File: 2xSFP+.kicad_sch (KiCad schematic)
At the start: 55 parts, among them J2 SFP+_Bel_SS-79100-010, U5 PCA9539AHF

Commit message: Update symbols from the library
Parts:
- J2: footprint antmicro-footprints:SFP_SS-79100-010 -> antmicro-footprints:SFP+_SS-79100-010
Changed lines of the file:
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@@
+    )
+  )
+  (symbol (lib_id "antmicroEdgeConnectors:SFP+_Bel_SS-79100-010") (at 261.62 60.96 0) (unit 1)
+    (in_bom yes) (on_board yes) (dnp no) (fields_autoplaced)
+    (property "Reference" "J2" (at 275.59 53.34 0)
+      (effects (font (size 1.27 1.27) (thickness 0.15)))
+    )
+    (property "Value" "SFP+_Bel_SS-79100-010" (at 303.53 73.66 0)
+      (effects (font (size 1.27 1.27) (thickness 0.15)) (justify left bottom) hide)
+    )
+    (property "Footprint" "antmicro-footprints:SFP+_SS-79100-010" (at 303.53 76.2 0)
+      (effects (font (size 1.27 1.27) (thickness 0.15)) (justify left bottom) hide)
+    )
+    (property "Datasheet" "https://www.belfuse.com/resources/datasheets/stewartconnector/ds-STW-SFP-cages.pdf" (at 303.53 78.74 0)
+      (effects (font (size 1.27 1.27) (thickness 0.15)) (justify left bottom) hide)
+    )
+    (property "MPN" "SS-79100-010" (at 275.59 55.88 0)
+      (effects (font (size 1.27 1.27) (thickness 0.15)))
+    )
+    (property "Manufacturer" "Bel Fuse" (at 303.53 68.58 0)
+      (effects (font (size 1.27 1.27) (thickness 0.15)) (justify left bottom) hide)
+    )
+    (property "Author" "Antmicro" (at 303.53 81.28 0)
+      (effects (font (size 1.27 1.27) (thickness 0.15)) (justify left bottom) hide)
+    )
+    (property "License" "Apache-2.0" (at 303.53 83.82 0)
+      (effects (font (size 1.27 1.27) (thickness 0.15)) (justify left bottom) hide)
+    )
+    (pin "B9")
+    (pin "T9")
+    (pin "B6")
+    (pin "B16")
+    (pin "T8")
+    (pin "B13")
+    (pin "T6")
+    (pin "B18")
+    (pin "B4")
+    (pin "B19")
+    (pin "T14")
+    (pin "T11")
+    (pin "T10")
+    (pin "T12")
+    (pin "T3")
+    (pin "B17")
+    (pin "T19")
+    (pin "T20")
+    (pin "B3")
+    (pin "B10")
+    (pin "B11")
+    (pin "T17")
+    (pin "T7")
+    (pin "B5")
+    (pin "B8")
+    (pin "B15")
+    (pin "B7")
+    (pin "T2")
+    (pin "T13")
+    (pin "T5")
+    (pin "T18")
+    (pin "B14")
+    (pin "B2")
+    (pin "B20")
+    (pin "T16")
+    (pin "T4")
+    (pin "B1")
+    (pin "T15")
+    (pin "B12")
+    (pin "SH")
+    (pin "T1")
+    (instances
+      (project "com-express-7-baseboard"
+        (path "/1b8c34da-dad5-4b0b-8c4b-45db766c4dfa/bc90cc14-34f1-4905-9b90-ab809e861ec6"
+          (reference "J2") (unit 1)
+        )
+      )
     )
   )
@@
     )
   )
-  (symbol (lib_id "antmicroEdgeConnectors:SFP+_Bel_SS-79100-010") (at 261.62 60.96 0) (unit 1)
-    (in_bom yes) (on_board yes) (dnp no) (fields_autoplaced)
-    (property "Reference" "J2" (at 275.59 53.34 0)
-      (effects (font (size 1.27 1.27) (thickness 0.15)))
-    )
-    (property "Value" "SFP+_Bel_SS-79100-010" (at 303.53 73.66 0)
-      (effects (font (size 1.27 1.27) (thickness 0.15)) (justify left bottom) hide)
-    )
-    (property "Footprint" "antmicro-footprints:SFP_SS-79100-010" (at 303.53 76.2 0)
-      (effects (font (size 1.27 1.27) (thickness 0.15)) (justify left bottom) hide)
-    )
-    (property "Datasheet" "https://www.belfuse.com/resources/datasheets/stewartconnector/ds-STW-SFP-cages.pdf" (at 303.53 78.74 0)
-      (effects (font (size 1.27 1.27) (thickness 0.15)) (justify left bottom) hide)
-    )
-    (property "MPN" "SS-79100-010" (at 275.59 55.88 0)
-      (effects (font (size 1.27 1.27) (thickness 0.15)))
-    )
-    (property "Manufacturer" "Bel Fuse" (at 303.53 68.58 0)
-      (effects (font (size 1.27 1.27) (thickness 0.15)) (justify left bottom) hide)
-    )
-    (property "Author" "Antmicro" (at 303.53 81.28 0)
-      (effects (font (size 1.27 1.27) (thickness 0.15)) (justify left bottom) hide)
-    )
-    (property "License" "Apache-2.0" (at 303.53 83.82 0)
-      (effects (font (size 1.27 1.27) (thickness 0.15)) (justify left bottom) hide)
-    )
-    (pin "T4")
-    (pin "B13")
-    (pin "B16")
-    (pin "B15")
-    (pin "B19")
-    (pin "B20")
-    (pin "T11")
-    (pin "B4")
-    (pin "B9")
-    (pin "B18")
-    (pin "B6")
-    (pin "T8")
-    (pin "B12")
-    (pin "B17")
-    (pin "T2")
-    (pin "B14")
-    (pin "B5")
-    (pin "B7")
-    (pin "T19")
-    (pin "B1")
-    (pin "T18")
-    (pin "B8")
-    (pin "T20")
-    (pin "B2")
-    (pin "T17")
-    (pin "T9")
-    (pin "T5")
-    (pin "T15")
-    (pin "T7")
-    (pin "B11")
-    (pin "T6")
-    (pin "B10")
-    (pin "T12")
-    (pin "T3")
-    (pin "T16")
-    (pin "B3")
-    (pin "T1")
-    (pin "T10")
-    (pin "SH")
-    (pin "T13")
-    (pin "T14")
-    (instances
-      (project "com-express-7-baseboard"
-        (path "/1b8c34da-dad5-4b0b-8c4b-45db766c4dfa/bc90cc14-34f1-4905-9b90-ab809e861ec6"
-          (reference "J2") (unit 1)
-        )
-      )
-    )
-  )
   (symbol (lib_id "antmicropower:+3V3") (at 322.58 69.85 0) (unit 1)
     (in_bom yes) (on_board yes) (dnp no)
@@
     )
   )
+  (symbol (lib_id "antmicroEdgeConnectors:SFP+_Bel_SS-79100-010") (at 261.62 144.78 0) (unit 2)
+    (in_bom yes) (on_board yes) (dnp no) (fields_autoplaced)
+    (property "Reference" "J2" (at 275.59 137.16 0)
+      (effects (font (size 1.27 1.27) (thickness 0.15)))
+    )
+    (property "Value" "SFP+_Bel_SS-79100-010" (at 303.53 157.48 0)
+      (effects (font (size 1.27 1.27) (thickness 0.15)) (justify left bottom) hide)
+    )
+    (property "Footprint" "antmicro-footprints:SFP+_SS-79100-010" (at 303.53 160.02 0)
+      (effects (font (size 1.27 1.27) (thickness 0.15)) (justify left bottom) hide)
+    )
+    (property "Datasheet" "https://www.belfuse.com/resources/datasheets/stewartconnector/ds-STW-SFP-cages.pdf" (at 303.53 162.56 0)
+      (effects (font (size 1.27 1.27) (thickness 0.15)) (justify left bottom) hide)
+    )
+    (property "MPN" "SS-79100-010" (at 275.59 139.7 0)
+      (effects (font (size 1.27 1.27) (thickness 0.15)))
+    )
+    (property "Manufacturer" "Bel Fuse" (at 303.53 152.4 0)
+      (effects (font (size 1.27 1.27) (thickness 0.15)) (justify left bottom) hide)
+    )
+    (property "Author" "Antmicro" (at 303.53 165.1 0)
+      (effects (font (size 1.27 1.27) (thickness 0.15)) (justify left bottom) hide)
+    )
+    (property "License" "Apache-2.0" (at 303.53 167.64 0)
+      (effects (font (size 1.27 1.27) (thickness 0.15)) (justify left bottom) hide)
+    )
+    (pin "B9")
+    (pin "T9")
+    (pin "B6")
+    (pin "B16")
+    (pin "T8")
+    (pin "B13")
+    (pin "T6")
+    (pin "B18")
+    (pin "B4")
+    (pin "B19")
+    (pin "T14")
+    (pin "T11")
+    (pin "T10")
+    (pin "T12")
+    (pin "T3")
+    (pin "B17")
+    (pin "T19")
+    (pin "T20")
+    (pin "B3")
+    (pin "B10")
+    (pin "B11")
+    (pin "T17")
+    (pin "T7")
+    (pin "B5")
+    (pin "B8")
+    (pin "B15")
+    (pin "B7")
+    (pin "T2")
+    (pin "T13")
+    (pin "T5")
+    (pin "T18")
+    (pin "B14")
+    (pin "B2")
+    (pin "B20")
+    (pin "T16")
+    (pin "T4")
+    (pin "B1")
+    (pin "T15")
+    (pin "B12")
+    (pin "SH")
+    (pin "T1")
+    (instances
+      (project "com-express-7-baseboard"
+        (path "/1b8c34da-dad5-4b0b-8c4b-45db766c4dfa/bc90cc14-34f1-4905-9b90-ab809e861ec6"
+          (reference "J2") (unit 2)
+        )
+      )
+    )
+  )
   (symbol (lib_id "antmicropower:GND") (at 177.8 274.32 0) (unit 1)
     (in_bom yes) (on_board yes) (dnp no)
@@
         )
       )
-    )
-  )
-  (symbol (lib_id "antmicroEdgeConnectors:SFP+_Bel_SS-79100-010") (at 261.62 144.78 0) (unit 2)
-    (in_bom yes) (on_board yes) (dnp no)
-    (property "Reference" "J2" (at 275.59 137.16 0)
-      (effects (font (size 1.27 1.27) (thickness 0.15)))
-    )
-    (property "Value" "SFP+_Bel_SS-79100-010" (at 303.53 157.48 0)
-      (effects (font (size 1.27 1.27) (thickness 0.15)) (justify left bottom) hide)
-    )
-    (property "Footprint" "antmicro-footprints:SFP_SS-79100-010" (at 303.53 160.02 0)
-      (effects (font (size 1.27 1.27) (thickness 0.15)) (justify left bottom) hide)
-    )
-    (property "Datasheet" "https://www.belfuse.com/resources/datasheets/stewartconnector/ds-STW-SFP-cages.pdf" (at 303.53 162.56 0)
-      (effects (font (size 1.27 1.27) (thickness 0.15)) (justify left bottom) hide)
-    )
-    (property "MPN" "SS-79100-010" (at 275.59 139.7 0)
-      (effects (font (size 1.27 1.27) (thickness 0.15)))
-    )
-    (property "Manufacturer" "Bel Fuse" (at 303.53 152.4 0)
-      (effects (font (size 1.27 1.27) (thickness 0.15)) (justify left bottom) hide)
-    )
-    (property "Author" "Antmicro" (at 303.53 165.1 0)
-      (effects (font (size 1.27 1.27) (thickness 0.15)) (justify left bottom) hide)
-    )
-    (property "License" "Apache-2.0" (at 303.53 167.64 0)
-      (effects (font (size 1.27 1.27) (thickness 0.15)) (justify left bottom) hide)
-    )
-    (pin "T4")
-    (pin "B13")
-    (pin "B16")
-    (pin "B15")
-    (pin "B19")
-    (pin "B20")
-    (pin "T11")
-    (pin "B4")
-    (pin "B9")
-    (pin "B18")
-    (pin "B6")
-    (pin "T8")
-    (pin "B12")
-    (pin "B17")
-    (pin "T2")
-    (pin "B14")
-    (pin "B5")
-    (pin "B7")
-    (pin "T19")
-    (pin "B1")
-    (pin "T18")
-    (pin "B8")
-    (pin "T20")
-    (pin "B2")
-    (pin "T17")
-    (pin "T9")
-    (pin "T5")
-    (pin "T15")
-    (pin "T7")
-    (pin "B11")
-    (pin "T6")
-    (pin "B10")
-    (pin "T12")
-    (pin "T3")
-    (pin "T16")
-    (pin "B3")
-    (pin "T1")
-    (pin "T10")
-    (pin "SH")
-    (pin "T13")
-    (pin "T14")
-    (instances
-      (project "com-express-7-baseboard"
-        (path "/1b8c34da-dad5-4b0b-8c4b-45db766c4dfa/bc90cc14-34f1-4905-9b90-ab809e861ec6"
-          (reference "J2") (unit 2)
-        )
-      )

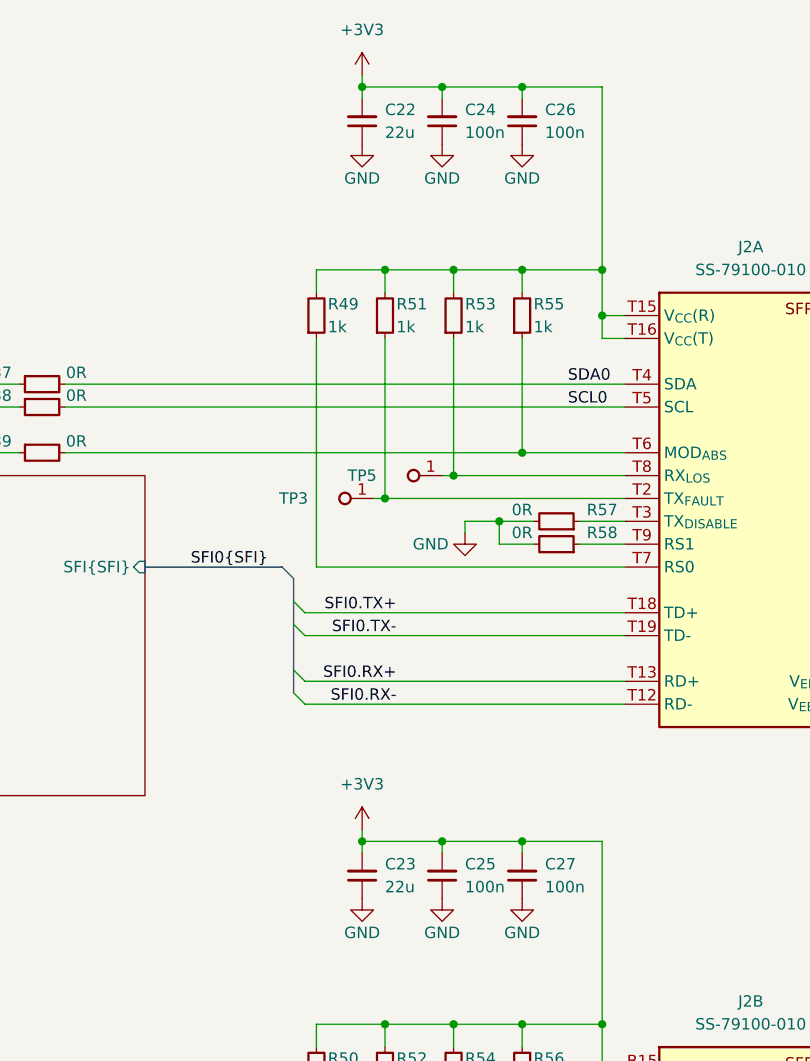
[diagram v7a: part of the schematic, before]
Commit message: [#58137] Add DC/DC supplies
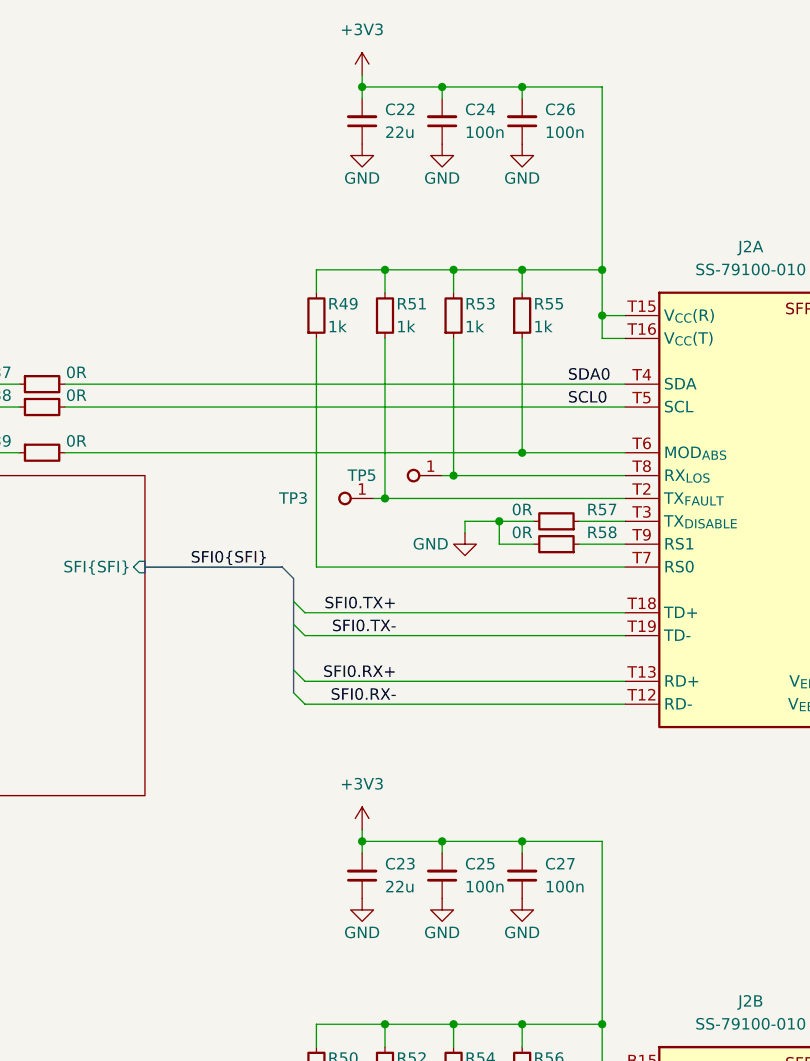
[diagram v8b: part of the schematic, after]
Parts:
- C22, C23: value C_22u_0603 -> C_22u_16V_0603; symbol antmicroCapacitors0603:C_22u_0603 -> antmicroCapacitors0603:C_22u_16V_0603; MPN GRM188R60J226MEA0D -> CL10A226MO7JZNC; Manufacturer Murata -> Samsung Electro-Mechanics; Voltage (none) -> 16V
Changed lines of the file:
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@@
     )
   )
-  (symbol (lib_id "antmicroCapacitors0603:C_22u_0603") (at 232.41 125.73 90) (unit 1)
+  (symbol (lib_id "antmicroCapacitors0603:C_22u_16V_0603") (at 232.41 125.73 90) (unit 1)
     (in_bom yes) (on_board yes) (dnp no) (fields_autoplaced)
-    (property "Reference" "C23" (at 234.95 121.9136 90)
-      (effects (font (size 1.27 1.27) (thickness 0.15)) (justify right))
-    )
-    (property "Value" "C_22u_0603" (at 242.57 105.41 0)
+    (property "Reference" "C23" (at 234.95 121.9135 90)
+      (effects (font (size 1.27 1.27) (thickness 0.15)) (justify right))
+    )
+    (property "Value" "C_22u_16V_0603" (at 242.57 105.41 0)
       (effects (font (size 1.27 1.27) (thickness 0.15)) (justify left bottom) hide)
     )
@@
       (effects (font (size 1.27 1.27) (thickness 0.15)) (justify left bottom) hide)
     )
-    (property "Datasheet" "https://www.murata.com/products/productdetail?partno=GRM188R60J226MEA0%23" (at 247.65 105.41 0)
-      (effects (font (size 1.27 1.27) (thickness 0.15)) (justify left bottom) hide)
-    )
-    (property "MPN" "GRM188R60J226MEA0D" (at 250.19 105.41 0)
-      (effects (font (size 1.27 1.27) (thickness 0.15)) (justify left bottom) hide)
-    )
-    (property "Manufacturer" "Murata" (at 252.73 105.41 0)
+    (property "Datasheet" "https://product.samsungsem.com/mlcc/CL10A226MO7JZN.do" (at 247.65 105.41 0)
+      (effects (font (size 1.27 1.27) (thickness 0.15)) (justify left bottom) hide)
+    )
+    (property "MPN" "CL10A226MO7JZNC" (at 250.19 105.41 0)
+      (effects (font (size 1.27 1.27) (thickness 0.15)) (justify left bottom) hide)
+    )
+    (property "Manufacturer" "Samsung Electro-Mechanics" (at 252.73 105.41 0)
       (effects (font (size 1.27 1.27) (thickness 0.15)) (justify left bottom) hide)
     )
@@
       (effects (font (size 1.27 1.27) (thickness 0.15)) (justify left bottom) hide)
     )
-    (property "Val" "22u" (at 234.95 124.4536 90)
-      (effects (font (size 1.27 1.27) (thickness 0.15)) (justify right))
-    )
-    (property "Voltage" "" (at 260.35 105.41 0)
+    (property "Val" "22u" (at 234.95 124.4535 90)
+      (effects (font (size 1.27 1.27) (thickness 0.15)) (justify right))
+    )
+    (property "Voltage" "16V" (at 260.35 105.41 0)
       (effects (font (size 1.27 1.27)) (justify left bottom) hide)
     )
@@
     )
   )
-  (symbol (lib_id "antmicroCapacitors0603:C_22u_0603") (at 232.41 41.91 90) (unit 1)
+  (symbol (lib_id "antmicroCapacitors0603:C_22u_16V_0603") (at 232.41 41.91 90) (unit 1)
     (in_bom yes) (on_board yes) (dnp no) (fields_autoplaced)
-    (property "Reference" "C22" (at 234.95 38.0936 90)
-      (effects (font (size 1.27 1.27) (thickness 0.15)) (justify right))
-    )
-    (property "Value" "C_22u_0603" (at 242.57 21.59 0)
+    (property "Reference" "C22" (at 234.95 38.0935 90)
+      (effects (font (size 1.27 1.27) (thickness 0.15)) (justify right))
+    )
+    (property "Value" "C_22u_16V_0603" (at 242.57 21.59 0)
       (effects (font (size 1.27 1.27) (thickness 0.15)) (justify left bottom) hide)
     )
@@
       (effects (font (size 1.27 1.27) (thickness 0.15)) (justify left bottom) hide)
     )
-    (property "Datasheet" "https://www.murata.com/products/productdetail?partno=GRM188R60J226MEA0%23" (at 247.65 21.59 0)
-      (effects (font (size 1.27 1.27) (thickness 0.15)) (justify left bottom) hide)
-    )
-    (property "MPN" "GRM188R60J226MEA0D" (at 250.19 21.59 0)
-      (effects (font (size 1.27 1.27) (thickness 0.15)) (justify left bottom) hide)
-    )
-    (property "Manufacturer" "Murata" (at 252.73 21.59 0)
+    (property "Datasheet" "https://product.samsungsem.com/mlcc/CL10A226MO7JZN.do" (at 247.65 21.59 0)
+      (effects (font (size 1.27 1.27) (thickness 0.15)) (justify left bottom) hide)
+    )
+    (property "MPN" "CL10A226MO7JZNC" (at 250.19 21.59 0)
+      (effects (font (size 1.27 1.27) (thickness 0.15)) (justify left bottom) hide)
+    )
+    (property "Manufacturer" "Samsung Electro-Mechanics" (at 252.73 21.59 0)
       (effects (font (size 1.27 1.27) (thickness 0.15)) (justify left bottom) hide)
     )
@@
       (effects (font (size 1.27 1.27) (thickness 0.15)) (justify left bottom) hide)
     )
-    (property "Val" "22u" (at 234.95 40.6336 90)
-      (effects (font (size 1.27 1.27) (thickness 0.15)) (justify right))
-    )
-    (property "Voltage" "" (at 260.35 21.59 0)
-      (effects (font (size 1.27 1.27)) (justify left bottom) hide)
-    )
+    (property "Val" "22u" (at 234.95 40.6335 90)
+      (effects (font (size 1.27 1.27) (thickness 0.15)) (justify right))
+    )
+    (property "Voltage" "16V" (at 260.35 21.59 0)
+      (effects (font (size 1.27 1.27)) (justify left bottom) hide)
+    )
